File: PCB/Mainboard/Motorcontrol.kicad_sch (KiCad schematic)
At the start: 29 parts, among them P1 TMC2209_Socket, P2 TMC2209_Socket, U5 PCA9685BS

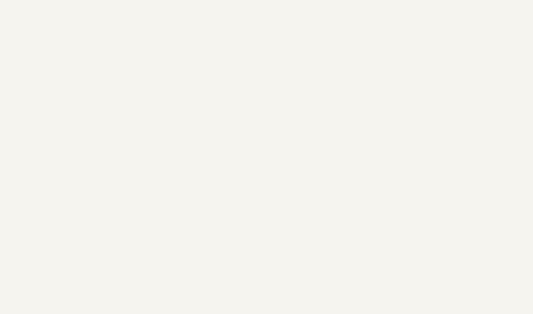
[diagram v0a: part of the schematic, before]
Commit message: Added setup, read and get Command
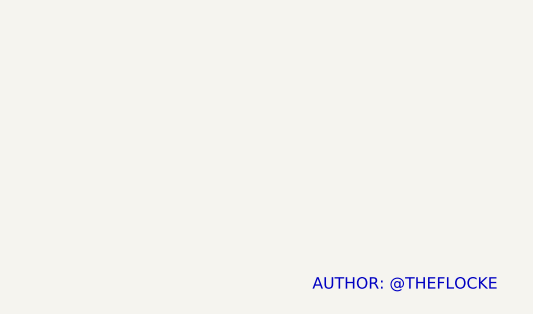
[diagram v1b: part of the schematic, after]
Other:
- note added: "AUTHOR: @THEFLOCKE"
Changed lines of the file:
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@@
+		)
+	)
+	(text "AUTHOR: @THEFLOCKE"
+		(exclude_from_sim no)
+		(at 249.936 196.596 0)
+		(effects
+			(font
+				(face "KiCad Font")
+				(size 1.27 1.27)
+				(color 194 0 194 1)
+			)
 		)
 	)
